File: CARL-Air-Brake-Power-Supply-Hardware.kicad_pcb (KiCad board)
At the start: 2 copper layers, 65 x 56 mm, 89 parts, among them J1 Battery, J2 ICSP, J3 USB, J4 Raspberry Pi, J5 Servo, SW1 Power, U1 TPS56528, U2 TPS56528, U3 FT232RNL, U4 ATmega328P-AU, Y1 16MHz

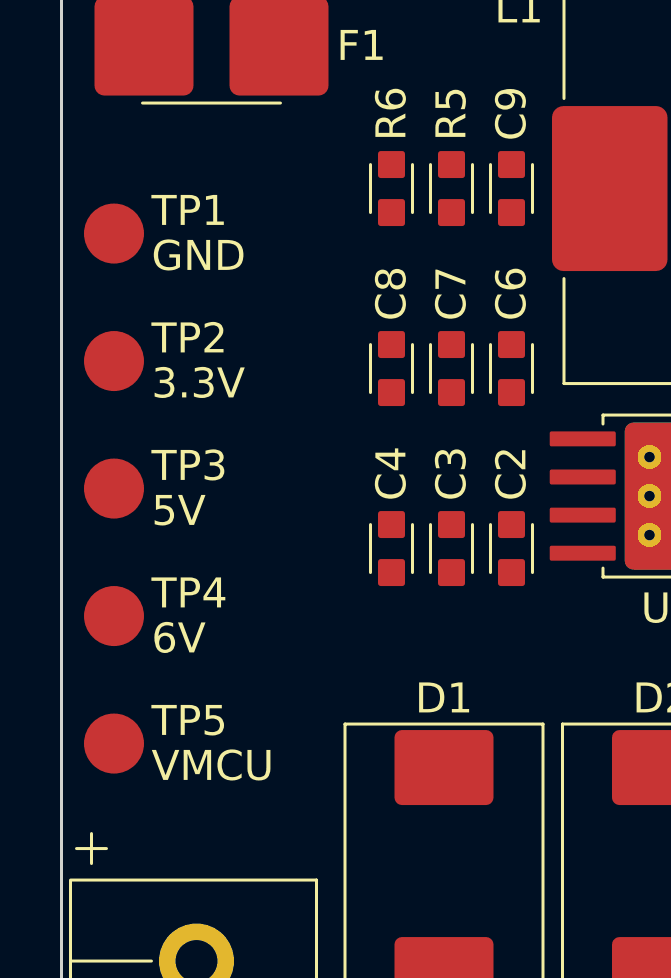
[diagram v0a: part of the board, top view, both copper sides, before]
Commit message: Added test point for VBAT
Added test point for VBAT line and updated PCB accordingly.
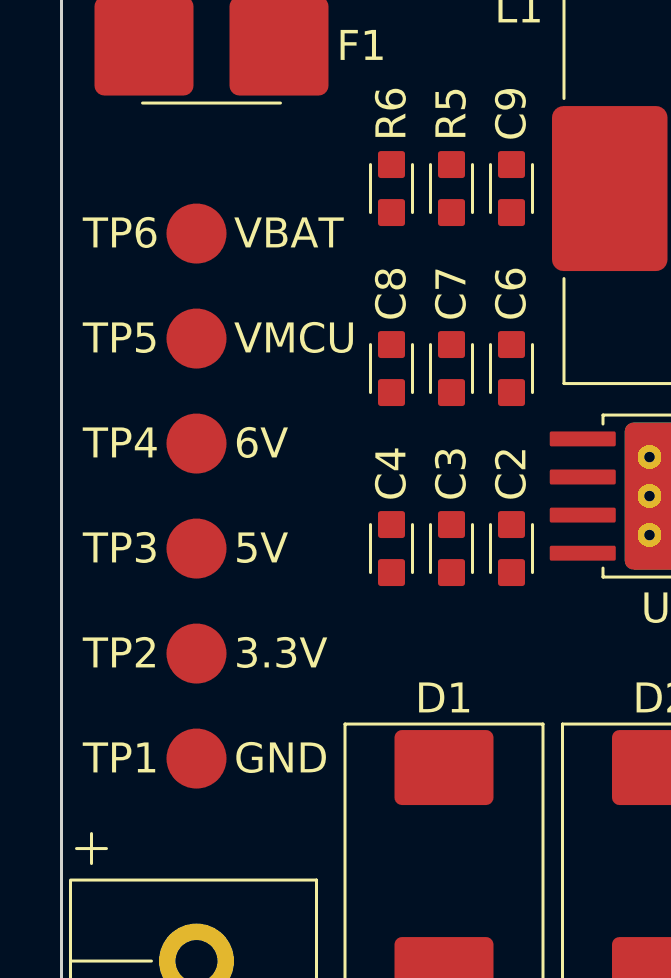
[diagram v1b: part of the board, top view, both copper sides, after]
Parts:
- added TP6: ~, Local_TestPoint:TestPoint_CircPad2.00mm_CircMsk2.50mm, F.Cu at (122.0, 87.5)
- moved TP1 17.7 mm to (122.0, 105.0)
- moved TP5 13.8 mm to (122.0, 91.0)
- moved TP2 10.1 mm to (122.0, 101.5)
- moved TP4 6.37 mm to (122.0, 94.5)
- moved TP3 3.40 mm to (122.0, 98.0)
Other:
- board text added: "VBAT"
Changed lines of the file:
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@@
   )
   (footprint "Local_TestPoint:TestPoint_CircPad2.00mm_CircMsk2.50mm" (layer "F.Cu")
-    (at 119.25 96)
-    (property "Sheetfile" "CARL-Air-Brake-Power-Supply-Hardware.kicad_sch")
-    (property "Sheetname" "")
-    (fp_text reference "TP3" (at 1.25 -0.75 unlocked) (layer "F.SilkS")
-        (effects (font (size 1 1) (thickness 0.1)) (justify left))
+    (at 122 98)
+    (property "Sheetfile" "CARL-Air-Brake-Power-Supply-Hardware.kicad_sch")
+    (property "Sheetname" "")
+    (fp_text reference "TP3" (at -1.25 0 unlocked) (layer "F.SilkS")
+        (effects (font (size 1 1) (thickness 0.1)) (justify right))
     )
     (fp_text value "~" (at 0 0 unlocked) (layer "F.Fab")
         (effects (font (size 1 1) (thickness 0.1)))
     )
-    (fp_text user "${REFERENCE}" (at 1.25 -0.75 unlocked) (layer "F.Fab")
-        (effects (font (size 1 1) (thickness 0.1)) (justify left))
+    (fp_text user "${REFERENCE}" (at -1.25 0 unlocked) (layer "F.Fab")
+        (effects (font (size 1 1) (thickness 0.1)) (justify right))
     )
     (pad "1" smd circle (at 0 0) (size 2 2) (layers "F.Cu" "F.Mask")
@@
   )
   (footprint "Local_TestPoint:TestPoint_CircPad2.00mm_CircMsk2.50mm" (layer "F.Cu")
-    (at 119.25 100.25)
-    (property "Sheetfile" "CARL-Air-Brake-Power-Supply-Hardware.kicad_sch")
-    (property "Sheetname" "")
-    (fp_text reference "TP4" (at 1.25 -0.75 unlocked) (layer "F.SilkS")
-        (effects (font (size 1 1) (thickness 0.1)) (justify left))
+    (at 122 94.5)
+    (property "Sheetfile" "CARL-Air-Brake-Power-Supply-Hardware.kicad_sch")
+    (property "Sheetname" "")
+    (fp_text reference "TP4" (at -1.25 0 unlocked) (layer "F.SilkS")
+        (effects (font (size 1 1) (thickness 0.1)) (justify right))
     )
     (fp_text value "~" (at 0 0 unlocked) (layer "F.Fab")
         (effects (font (size 1 1) (thickness 0.1)))
     )
-    (fp_text user "${REFERENCE}" (at 1.25 -0.75 unlocked) (layer "F.Fab")
-        (effects (font (size 1 1) (thickness 0.1)) (justify left))
+    (fp_text user "${REFERENCE}" (at -1.25 0 unlocked) (layer "F.Fab")
+        (effects (font (size 1 1) (thickness 0.1)) (justify right))
     )
     (pad "1" smd circle (at 0 0) (size 2 2) (layers "F.Cu" "F.Mask")
@@
   )
   (footprint "Local_TestPoint:TestPoint_CircPad2.00mm_CircMsk2.50mm" (layer "F.Cu")
-    (at 119.25 87.5)
-    (property "Sheetfile" "CARL-Air-Brake-Power-Supply-Hardware.kicad_sch")
-    (property "Sheetname" "")
-    (fp_text reference "TP1" (at 1.25 -0.75 unlocked) (layer "F.SilkS")
-        (effects (font (size 1 1) (thickness 0.1)) (justify left))
+    (at 122 105)
+    (property "Sheetfile" "CARL-Air-Brake-Power-Supply-Hardware.kicad_sch")
+    (property "Sheetname" "")
+    (fp_text reference "TP1" (at -1.25 0 unlocked) (layer "F.SilkS")
+        (effects (font (size 1 1) (thickness 0.1)) (justify right))
     )
     (fp_text value "~" (at 0 0 unlocked) (layer "F.Fab")
         (effects (font (size 1 1) (thickness 0.1)))
     )
-    (fp_text user "${REFERENCE}" (at 1.25 -0.75 unlocked) (layer "F.Fab")
-        (effects (font (size 1 1) (thickness 0.1)) (justify left))
+    (fp_text user "${REFERENCE}" (at -1.25 0 unlocked) (layer "F.Fab")
+        (effects (font (size 1 1) (thickness 0.1)) (justify right))
     )
     (pad "1" smd circle (at 0 0) (size 2 2) (layers "F.Cu" "F.Mask")
@@
       (solder_mask_margin 1.625))
   )
+  (footprint "Local_TestPoint:TestPoint_CircPad2.00mm_CircMsk2.50mm" (layer "F.Cu")
+    (at 122 87.5)
+    (property "Sheetfile" "CARL-Air-Brake-Power-Supply-Hardware.kicad_sch")
+    (property "Sheetname" "")
+    (fp_text reference "TP6" (at -1.25 0 unlocked) (layer "F.SilkS")
+        (effects (font (size 1 1) (thickness 0.1)) (justify right))
+    )
+    (fp_text value "~" (at 0 0 unlocked) (layer "F.Fab")
+        (effects (font (size 1 1) (thickness 0.1)))
+    )
+    (fp_text user "${REFERENCE}" (at -1.25 0 unlocked) (layer "F.Fab")
+        (effects (font (size 1 1) (thickness 0.1)) (justify right))
+    )
+    (pad "1" smd circle (at 0 0) (size 2 2) (layers "F.Cu" "F.Mask")
+      (net 3 "VBAT") (pintype "passive") (solder_mask_margin 0.25) (clearance 0.25))
+  )
   (footprint "Local_Resistor_SMD:Res_Film_0603" (layer "F.Cu")
     (at 128.5 86 90)
@@
   )
   (footprint "Local_TestPoint:TestPoint_CircPad2.00mm_CircMsk2.50mm" (layer "F.Cu")
-    (at 119.25 104.5)
-    (property "Sheetfile" "CARL-Air-Brake-Power-Supply-Hardware.kicad_sch")
-    (property "Sheetname" "")
-    (fp_text reference "TP5" (at 1.25 -0.75 unlocked) (layer "F.SilkS")
-        (effects (font (size 1 1) (thickness 0.1)) (justify left))
+    (at 122 91)
+    (property "Sheetfile" "CARL-Air-Brake-Power-Supply-Hardware.kicad_sch")
+    (property "Sheetname" "")
+    (fp_text reference "TP5" (at -1.25 0 unlocked) (layer "F.SilkS")
+        (effects (font (size 1 1) (thickness 0.1)) (justify right))
     )
     (fp_text value "~" (at 0 0 unlocked) (layer "F.Fab")
         (effects (font (size 1 1) (thickness 0.1)))
     )
-    (fp_text user "${REFERENCE}" (at 1.25 -0.75 unlocked) (layer "F.Fab")
-        (effects (font (size 1 1) (thickness 0.1)) (justify left))
+    (fp_text user "${REFERENCE}" (at -1.25 0 unlocked) (layer "F.Fab")
+        (effects (font (size 1 1) (thickness 0.1)) (justify right))
     )
     (pad "1" smd circle (at 0 0) (size 2 2) (layers "F.Cu" "F.Mask")
@@
   )
   (footprint "Local_TestPoint:TestPoint_CircPad2.00mm_CircMsk2.50mm" (layer "F.Cu")
-    (at 119.25 91.75)
-    (property "Sheetfile" "CARL-Air-Brake-Power-Supply-Hardware.kicad_sch")
-    (property "Sheetname" "")
-    (fp_text reference "TP2" (at 1.25 -0.75 unlocked) (layer "F.SilkS")
-        (effects (font (size 1 1) (thickness 0.1)) (justify left))
+    (at 122 101.5)
+    (property "Sheetfile" "CARL-Air-Brake-Power-Supply-Hardware.kicad_sch")
+    (property "Sheetname" "")
+    (fp_text reference "TP2" (at -1.25 0 unlocked) (layer "F.SilkS")
+        (effects (font (size 1 1) (thickness 0.1)) (justify right))
     )
     (fp_text value "~" (at 0 0 unlocked) (layer "F.Fab")
         (effects (font (size 1 1) (thickness 0.1)))
     )
-    (fp_text user "${REFERENCE}" (at 1.25 -0.75 unlocked) (layer "F.Fab")
-        (effects (font (size 1 1) (thickness 0.1)) (justify left))
+    (fp_text user "${REFERENCE}" (at -1.25 0 unlocked) (layer "F.Fab")
+        (effects (font (size 1 1) (thickness 0.1)) (justify right))
     )
     (pad "1" smd circle (at 0 0) (size 2 2) (layers "F.Cu" "F.Mask")
@@
     (effects (font (size 1 1) (thickness 0.1)) (justify right))
   )
-  (gr_text "3.3V" (at 120.5 92.5) (layer "F.SilkS")
+  (gr_text "3.3V" (at 123.25 101.5) (layer "F.SilkS")
     (effects (font (size 1 1) (thickness 0.1)) (justify left))
   )
@@
     (effects (font (size 1 1) (thickness 0.1)) (justify right))
   )
-  (gr_text "GND" (at 120.5 88.25) (layer "F.SilkS")
+  (gr_text "GND" (at 123.25 105) (layer "F.SilkS")
     (effects (font (size 1 1) (thickness 0.1)) (justify left))
   )
@@
     (effects (font (size 1 1) (thickness 0.1)))
   )
-  (gr_text "VMCU" (at 120.5 105.25) (layer "F.SilkS")
+  (gr_text "VMCU" (at 123.25 91) (layer "F.SilkS")
     (effects (font (size 1 1) (thickness 0.1)) (justify left))
   )
@@
     (effects (font (size 1 1) (thickness 0.1)) (justify right))
   )
-  (gr_text "6V" (at 120.5 101) (layer "F.SilkS")
+  (gr_text "6V" (at 123.25 94.5) (layer "F.SilkS")
     (effects (font (size 1 1) (thickness 0.1)) (justify left))
   )
@@
     (effects (font (size 1 1) (thickness 0.1)) (justify left))
   )
+  (gr_text "VBAT" (at 123.25 87.5) (layer "F.SilkS")
+    (effects (font (size 1 1) (thickness 0.1)) (justify left))
+  )
   (gr_text "MOSI" (at 154 123.5) (layer "F.SilkS")
     (effects (font (size 1 1) (thickness 0.1)) (justify left))
@@
     (effects (font (size 1 1) (thickness 0.1)) (justify right))
   )
-  (gr_text "5V" (at 120.5 96.75) (layer "F.SilkS")
+  (gr_text "5V" (at 123.25 98) (layer "F.SilkS")
     (effects (font (size 1 1) (thickness 0.1)) (justify left))
   )
@@
   )
   (dimension (type aligned) (layer "Dwgs.User")
-    (pts (xy 120.999999 72) (xy 120.999999 128))
+    (pts (xy 120.999999 70) (xy 120.999999 126))
     (height 4.999999)
-    (gr_text "56.00 mm" (at 114.9 100 90) (layer "Dwgs.User")
+    (gr_text "56.00 mm" (at 114.9 98 90) (layer "Dwgs.User")
       (effects (font (size 1 1) (thickness 0.1)))
     )

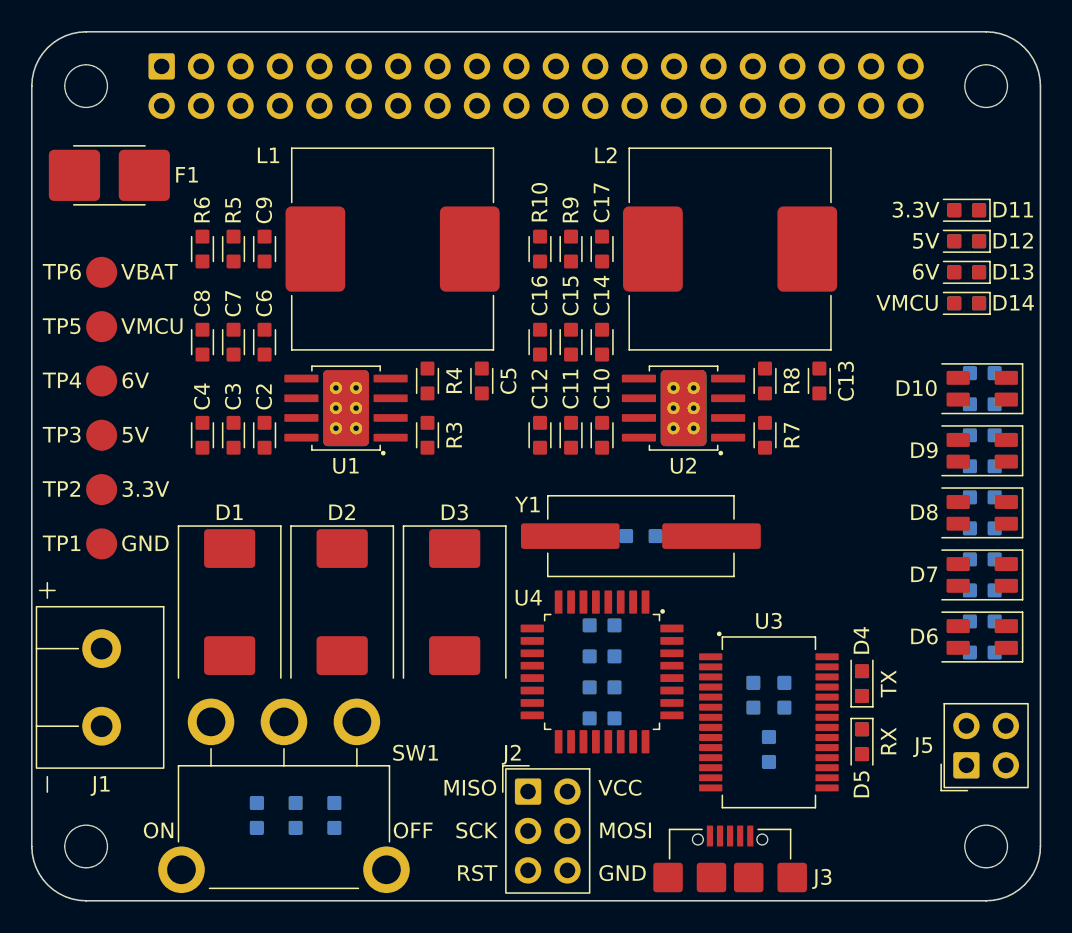
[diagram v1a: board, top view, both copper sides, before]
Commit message: Added filled zones
Added filled copper zones for high current power supply lines.
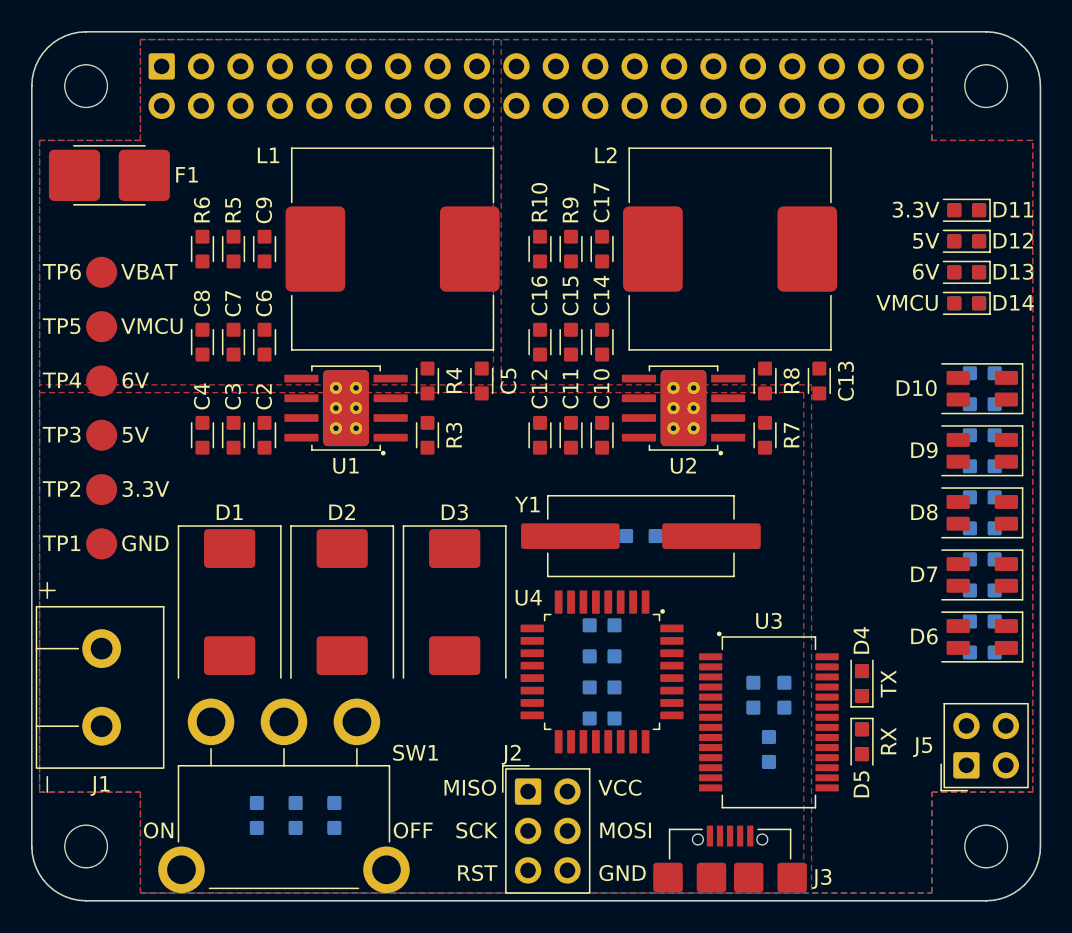
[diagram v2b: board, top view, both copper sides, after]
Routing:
- added copper zone on F.Cu, net +5V
- added copper zone on F.Cu, net +6V
- added copper zone on B.Cu, net GND
- added copper zone on F.Cu, net VBAT
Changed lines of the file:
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@@
     (style (thickness 0.1) (arrow_length 1) (text_position_mode 2) (extension_height 0.58642) (extension_offset 0) keep_text_aligned)
   )
+  (zone (net 3) (net_name "VBAT") (layer "F.Cu") (name "VBAT") (hatch edge 0.5)
+    (priority 1)
+    (connect_pads (clearance 0.2))
+    (min_thickness 0.2) (filled_areas_thickness no)
+    (fill (thermal_gap 0.2) (thermal_bridge_width 0.4) (smoothing fillet) (radius 0.5))
+    (polygon
+      (pts
+        (xy 124.5 121)
+        (xy 118 121)
+        (xy 118 95.25)
+        (xy 167.25 95.25)
+        (xy 167.25 127.5)
+        (xy 124.5 127.5)
+      )
+    )
+  )
+  (zone (net 7) (net_name "+5V") (layer "F.Cu") (name "+5V") (hatch edge 0.5)
+    (priority 2)
+    (connect_pads (clearance 0.2))
+    (min_thickness 0.2) (filled_areas_thickness no)
+    (fill (thermal_gap 0.2) (thermal_bridge_width 0.4) (smoothing fillet) (radius 0.5))
+    (polygon
+      (pts
+        (xy 118 94.75)
+        (xy 118 79)
+        (xy 124.5 79)
+        (xy 124.5 72.5)
+        (xy 147.25 72.5)
+        (xy 147.25 94.75)
+      )
+    )
+  )
+  (zone (net 12) (net_name "+6V") (layer "F.Cu") (name "+6V") (hatch edge 0.5)
+    (priority 3)
+    (connect_pads (clearance 0.2))
+    (min_thickness 0.2) (filled_areas_thickness no)
+    (fill (thermal_gap 0.2) (thermal_bridge_width 0.4) (smoothing fillet) (radius 0.5))
+    (polygon
+      (pts
+        (xy 147.75 72.5)
+        (xy 147.75 94.75)
+        (xy 167.75 94.75)
+        (xy 167.75 127.5)
+        (xy 175.5 127.5)
+        (xy 175.5 121)
+        (xy 182 121)
+        (xy 182 79)
+        (xy 175.5 79)
+        (xy 175.5 72.5)
+      )
+    )
+  )
+  (zone (net 1) (net_name "GND") (layer "B.Cu") (name "GND") (hatch edge 0.5)
+    (connect_pads (clearance 0.2))
+    (min_thickness 0.2) (filled_areas_thickness no)
+    (fill (thermal_gap 0.2) (thermal_bridge_width 0.4) (smoothing fillet) (radius 0.5))
+    (polygon
+      (pts
+        (xy 124.5 72.5)
+        (xy 124.5 79)
+        (xy 118 79)
+        (xy 118 121)
+        (xy 124.5 121)
+        (xy 124.5 127.5)
+        (xy 175.5 127.5)
+        (xy 175.5 121)
+        (xy 182 121)
+        (xy 182 79)
+        (xy 175.5 79)
+        (xy 175.5 72.5)
+      )
+    )
+  )
 )

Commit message: Routed circuit board
Completed circuit design by routing all connections, and performed DRC.
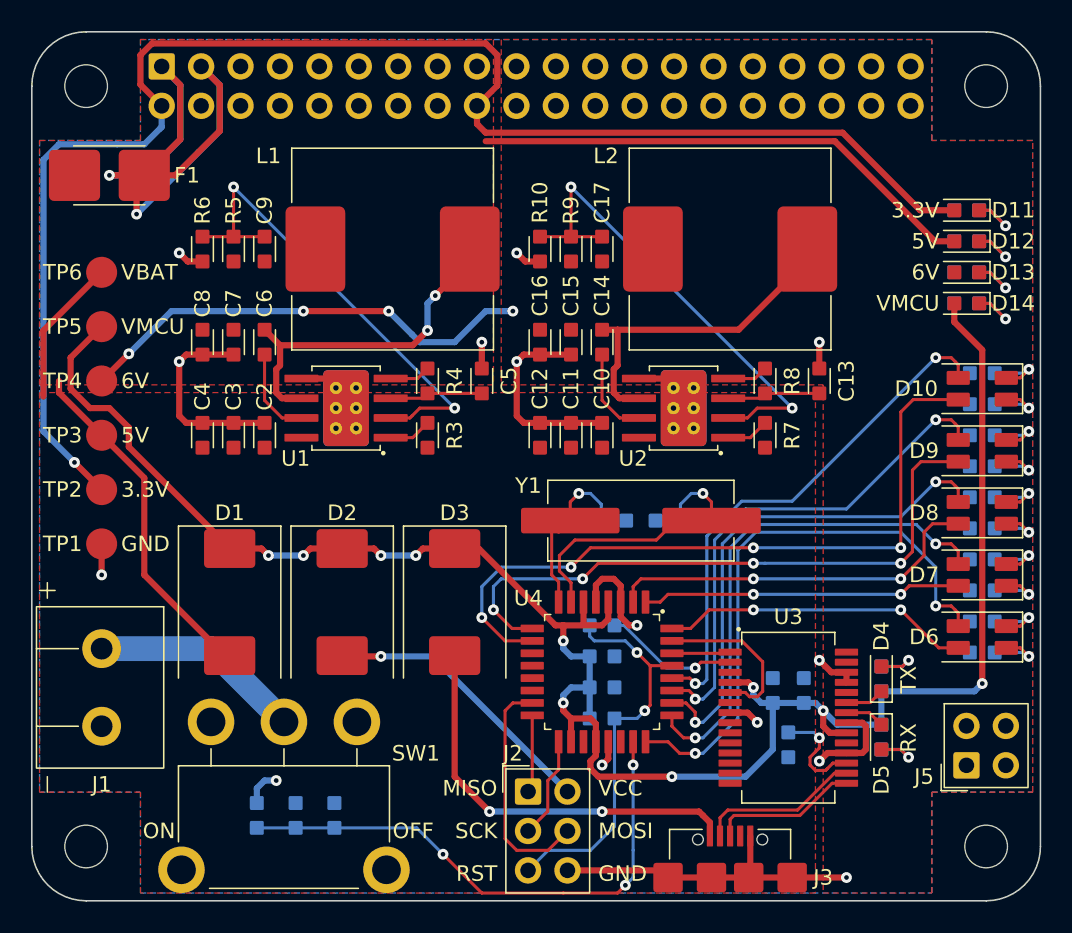
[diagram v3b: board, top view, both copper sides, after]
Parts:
- moved C21 4.00 mm to (154.2, 114.2)
- moved C23 4.00 mm to (154.2, 110.2), turned to 0 degrees
- moved C18 1.29 mm to (165.2, 114.5)
- moved C19 1.29 mm to (167.2, 114.5)
- moved C20 1.29 mm to (166.2, 118.0)
- moved D4 1.29 mm to (172.2, 113.7)
- moved D5 1.29 mm to (172.2, 117.5)
- moved R11 1.29 mm to (172.2, 113.7)
- moved R12 1.29 mm to (172.2, 117.5)
- moved U3 1.29 mm to (166.2, 116.2)
- moved C24 1.00 mm to (155.0, 103.5)
- moved C25 1.00 mm to (158.5, 103.5)
- moved Y1 1.00 mm to (156.8, 103.5)
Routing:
- net VBUS: track 0.00 -> 131.0 mm, vias 0 -> 10
- net +3.3V: track 0.00 -> 98.2 mm, vias 0 -> 1
- net GND: track 0.00 -> 79.3 mm, vias 0 -> 13
- net +5V: track 0.00 -> 55.3 mm
- net /5V_RPI: track 0.00 -> 47.1 mm, vias 0 -> 2
- net /RLED5: track 0.00 -> 46.7 mm, vias 0 -> 4
- net /RLED4: track 0.00 -> 40.9 mm, vias 0 -> 4
- net /GLED1: track 0.00 -> 37.2 mm, vias 0 -> 2
- net /BATT_LEV: track 0.00 -> 35.2 mm, vias 0 -> 3
- net /GLED5: track 0.00 -> 33.7 mm, vias 0 -> 2
- net /GLED2: track 0.00 -> 32.9 mm, vias 0 -> 2
- net /GLED4: track 0.00 -> 32.8 mm, vias 0 -> 2
- net /GLED3: track 0.00 -> 32.8 mm, vias 0 -> 2
- net Net-(U2-VFB): track 0.00 -> 31.7 mm, vias 0 -> 2
- net Net-(U1-VFB): track 0.00 -> 31.7 mm, vias 0 -> 2
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
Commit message: Changed VBUS to VMCU
Changed name of VBUS net to VMCU in schematic and board files.
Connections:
- net /VBUS_ICSP renamed /VMCU_ICSP
- net /VBUS_USB renamed /VMCU_USB
- net VBUS renamed VMCU

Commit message: Corrected component values
Corrected resistance values of resistors R6 and R10.
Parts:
- R10, R6: value 365kOhm -> 50kOhm
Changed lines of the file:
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@@
         (effects (font (size 1 1) (thickness 0.1)))
     )
-    (fp_text value "365kOhm" (at 0 0 90 unlocked) (layer "F.Fab")
+    (fp_text value "50kOhm" (at 0 0 90 unlocked) (layer "F.Fab")
         (effects (font (size 1 1) (thickness 0.1)))
     )
@@
         (effects (font (size 1 1) (thickness 0.1)))
     )
-    (fp_text value "365kOhm" (at 0 0 90 unlocked) (layer "F.Fab")
-        (effects (font (size 1 1) (thickness 0.1)))
-    )
+    (fp_text value "50kOhm" (at 0 0 90 unlocked) (layer "F.Fab")
+        (effects (font (size 1 1) (thickness 0.1)))
+    )
